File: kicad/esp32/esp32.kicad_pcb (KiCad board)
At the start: 2 copper layers, 67.5 x 101.7 mm, 42 parts, among them J101 RJ45, J102 NodeMCU, J103 Annunciator, SW201 B3F-1150, SW301 B3F-1150, SW401 B3F-1150, U101 74LS14, X101 Mouse Bites, X102 Mouse Bites, X103 Mouse Bites, X104 Mouse Bites

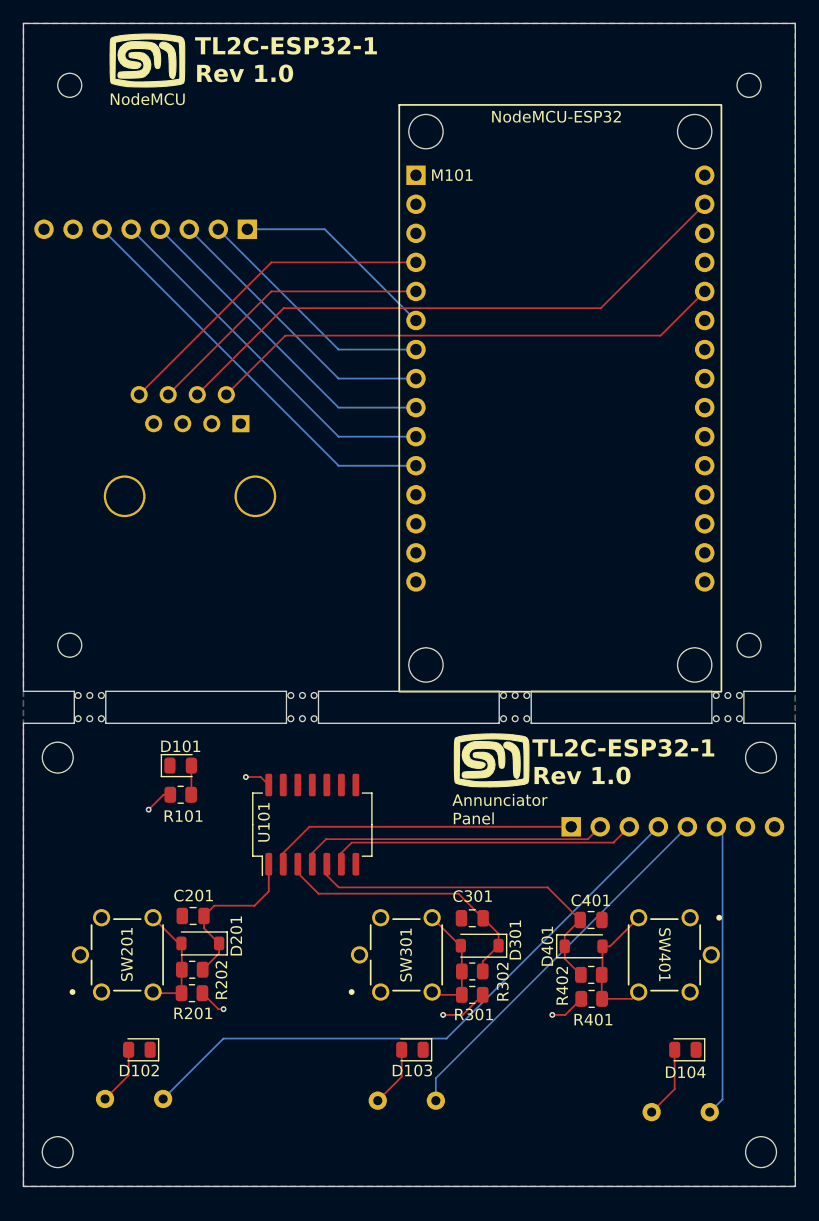
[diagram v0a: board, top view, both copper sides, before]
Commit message: Created the front panel artwork with drill marks
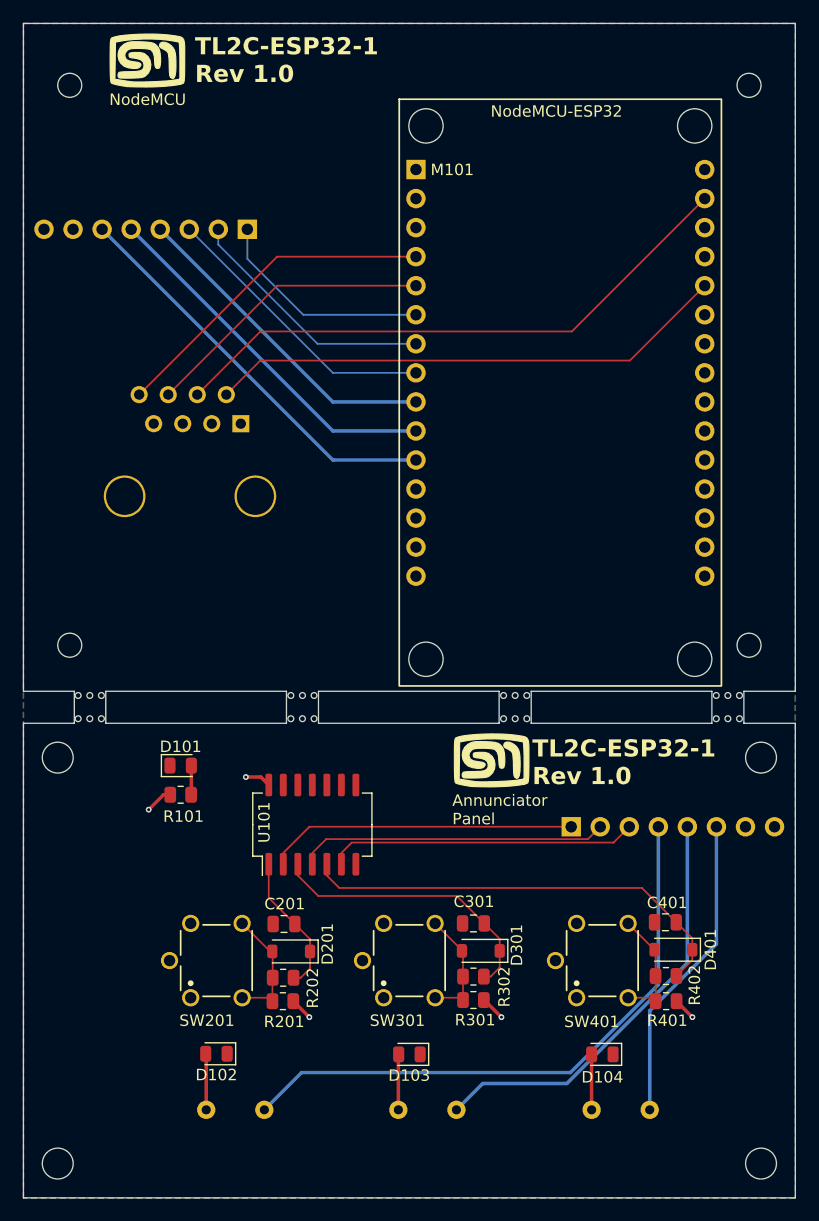
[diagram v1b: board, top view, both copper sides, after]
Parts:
- moved SW201 10.4 mm to (41.9, 107.0)
- moved R102 8.90 mm to (41.0, 120.0)
- moved SW401 8.54 mm to (75.6, 107.0), turned to 90 degrees
- moved D201 7.98 mm to (48.4, 106.2)
- moved R201 7.98 mm to (47.7, 110.5)
- moved C201 7.98 mm to (47.8, 103.8)
- moved R202 7.98 mm to (47.7, 108.5)
- moved D401 7.86 mm to (81.8, 106.0), turned to 180 degrees
- moved D104 7.27 mm to (75.6, 115.1)
- moved D102 6.75 mm to (41.9, 115.1)
- moved R402 6.53 mm to (81.2, 108.3), turned to 180 degrees
- moved R401 6.52 mm to (81.2, 110.5), turned to 180 degrees
- moved C401 6.50 mm to (81.1, 103.6), turned to 180 degrees
- moved R104 5.25 mm to (74.7, 120.0)
- moved SW301 3.72 mm to (58.8, 107.0)
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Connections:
- J101 pad 1: unconnected-(J101-Pad1) -> GND
- J101 pad 3: unconnected-(J101-Pad3) -> GND
- J101 pad 5: unconnected-(J101-Pad5) -> GND
- J101 pad 7: unconnected-(J101-Pad7) -> GND
- U101 pad 10: (no net) -> unconnected-(U101-Pad10)
- U101 pad 11: (no net) -> unconnected-(U101-Pad11)
- U101 pad 12: (no net) -> unconnected-(U101-Pad12)
- U101 pad 13: (no net) -> unconnected-(U101-Pad13)
- U101 pad 8: (no net) -> unconnected-(U101-Pad8)
- U101 pad 9: (no net) -> unconnected-(U101-Pad9)
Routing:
- net /Zone 3 Enable/ZONE_GPIO: track 30.7 -> 39.1 mm
- net /Zone2_ACTIVE: track 65.5 -> 69.6 mm
- net +3V3: track 14.4 -> 10.8 mm
- net /Zone 1 Enable/ZONE_GPIO: track 14.8 -> 12.4 mm
- net Net-(D401-A): track 12.3 -> 10.3 mm
- net Net-(D104-A): track 6.28 -> 4.85 mm
- net /Zone3_ACTIVE: track 61.6 -> 63.0 mm
- net /ZONE3_BTN: track 52.3 -> 51.1 mm
- net /Zone 2 Enable/ZONE_GPIO: track 24.4 -> 25.2 mm
- net /Zone1_ACTIVE: track 82.0 -> 81.4 mm
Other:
- board size 67.5 x 101.7 mm -> 67.5 x 102.7 mm
- board text added: "1"
- board text added: "2"
- board text added: "3"
- board text added: "TL2C ESP32 1"
- board text added: "ZONES"

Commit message: Pin reassignments after starting the firmware
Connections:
- M101 pad 10: /Zone2_ACTIVE -> unconnected-(M101-TOUCH7/ADC17/D27-Pad10)
- M101 pad 11: /Zone3_ACTIVE -> /Zone1_ACTIVE
- M101 pad 13: unconnected-(M101-SPI-MISO/TOUCH4/ADC14/D13-Pad13) -> /Zone2_ACTIVE
- M101 pad 18: unconnected-(M101-SPI-SS/TOUCH3/ADC13/D15-Pad18) -> /Zone3_ACTIVE
- M101 pad 4: /~{SLEEP} -> unconnected-(M101-ADC6/D34-Pad4)
- M101 pad 5: /STATE_INTERRUPT -> /~{SLEEP}
- M101 pad 6: /ZONE1_BTN -> /STATE_INTERRUPT
- M101 pad 7: /ZONE2_BTN -> /ZONE1_BTN
- M101 pad 8: /ZONE3_BTN -> /ZONE2_BTN
- M101 pad 9: /Zone1_ACTIVE -> /ZONE3_BTN
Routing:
- net /Zone3_ACTIVE: track 63.0 -> 91.5 mm
- net /Zone2_ACTIVE: track 69.6 -> 73.0 mm
- net /Zone1_ACTIVE: track 81.4 -> 83.5 mm
- net /~{SLEEP}: track 29.2 -> 28.2 mm
- net /ZONE3_BTN: track 51.1 -> 52.2 mm
- net /STATE_INTERRUPT: track 25.6 -> 24.6 mm

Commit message: Completed the release for OSH Park
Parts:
- moved Lg102 1.99 mm to (64.0, 90.0)
- moved H103 1.36 mm to (88.5, 78.0)
- moved H104 1.36 mm to (29.1, 78.0)
- moved H106 1.22 mm to (29.0, 124.0)
- moved H107 1.22 mm to (88.5, 124.0)
- moved H105 1.12 mm to (29.0, 89.7)
- moved H108 1.12 mm to (88.5, 89.7)
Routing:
- net /ZONE2_BTN: track 48.6 -> 52.4 mm
- net /ZONE3_BTN: track 52.2 -> 55.7 mm
- net /ZONE1_BTN: track 45.1 -> 47.3 mm
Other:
- board text added: "Test Mode"

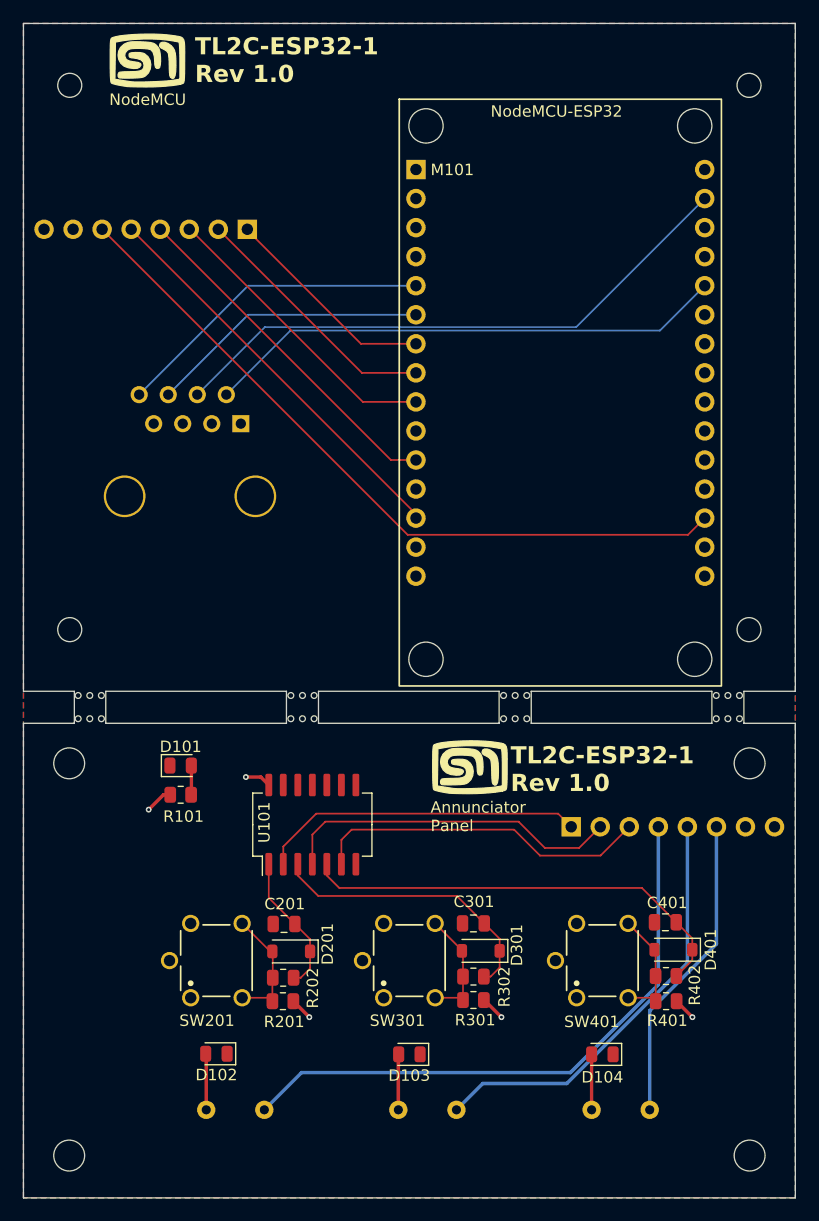
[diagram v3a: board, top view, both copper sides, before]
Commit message: Created rev 1.01 - Addes some more labels and annotations
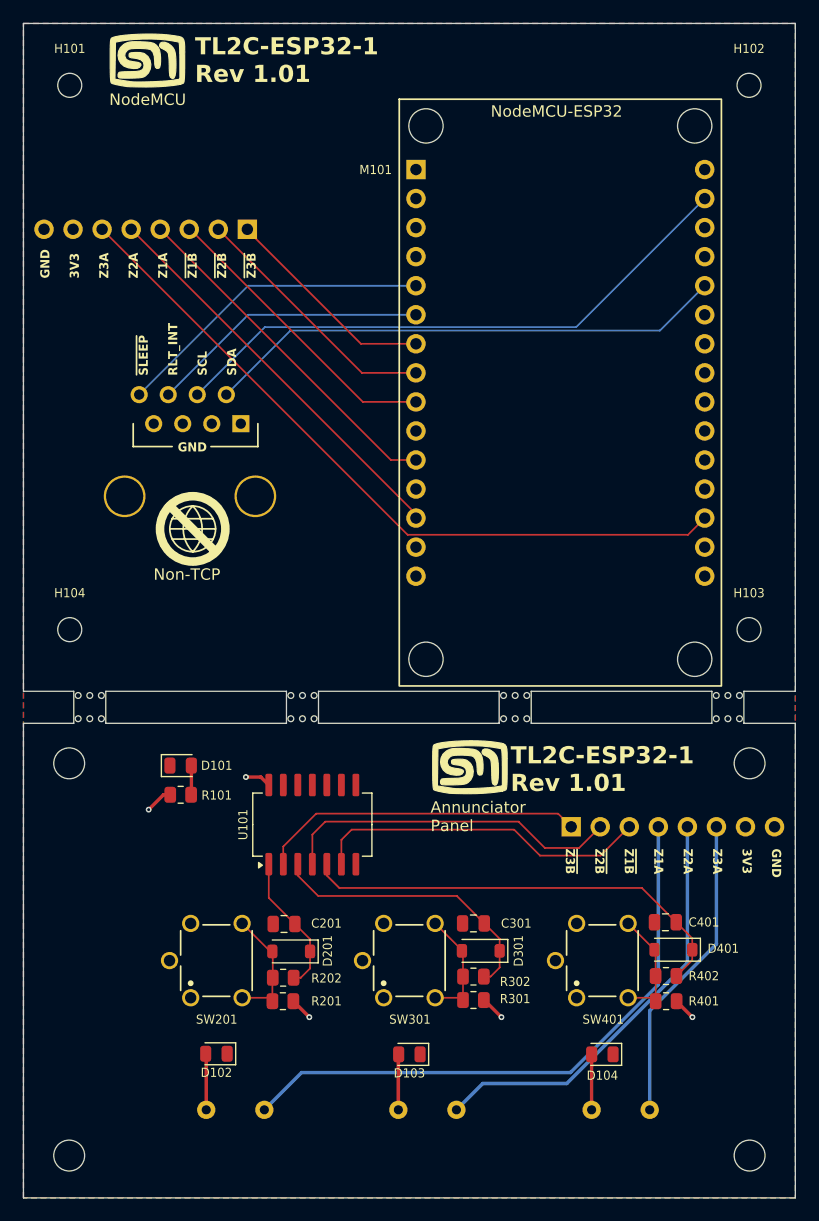
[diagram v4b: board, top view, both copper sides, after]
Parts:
- added Lg103: SM Logo, sjm-mechanical:MyBasic_rounded_50_1_USER5, F.Cu at (36.0, 90.4)
- added Lg104: Non-TCP, sjm-mechanical:Non_TCP, F.Cu at (39.8, 69.2)
- added Lg105: Non-TCP, sjm-mechanical:Non_TCP, B.Cu at (39.7, 78.1)
- added Lg106: SM Logo, sjm-mechanical:MyBasic_rounded_50_1, B.Cu at (80.0, 28.3)
- added Lg107: SM Logo, sjm-mechanical:MyBasic_rounded_50_1, B.Cu at (81.5, 90.0)
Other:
- board text added: "GND"
- board text added: "GND 3V3 Z3A Z2A Z1A ~{Z1B} ~{Z2B} ~{Z3B}"
- board text added: "TL2C ESP32-1"
- board text added: "TL2C-ESP32-1 Rev 1.01"
- board text added: "~{SLEEP} RLT_INT SCL SDA"
- board text removed: "TL2C ESP32 1"
- board text removed: "TL2C-ESP32-1 Rev 1.0"

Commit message: Reseated the RJ45
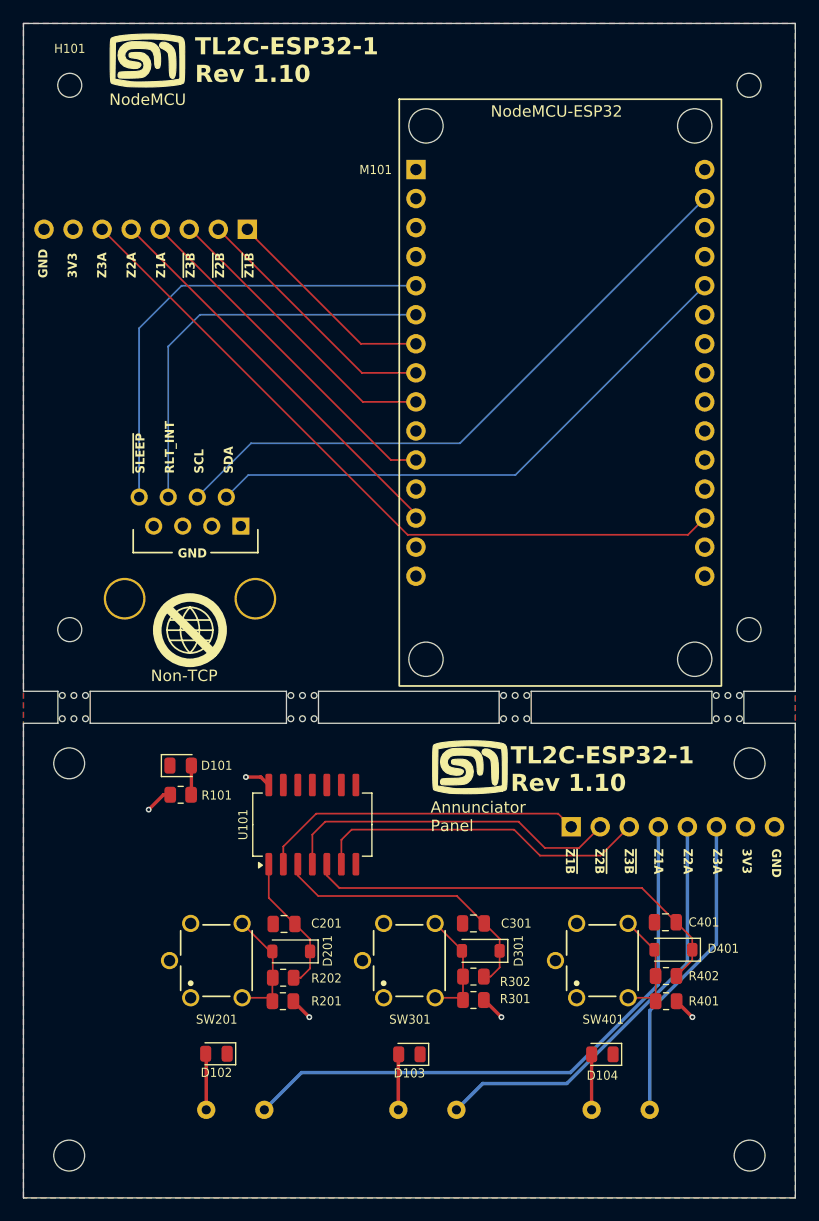
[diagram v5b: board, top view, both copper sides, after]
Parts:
- R201, R301, R401: value 51κΩ -> 47κΩ
- R202, R302, R402: value 21kΩ -> 470Ω
- moved J101 8.96 mm to (35.1, 66.4)
- moved Lg104 8.86 mm to (39.6, 78.1)
- moved X101 1.39 mm to (29.4, 84.8)
- moved Lg105 0.15 mm to (39.6, 78.1)
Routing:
- net /~{SLEEP}: track 28.2 -> 40.5 mm
- net /STATE_INTERRUPT: track 24.6 -> 36.0 mm
- net /I2C_SDA: track 45.8 -> 49.5 mm
- net /I2C_SCL: track 51.5 -> 55.2 mm
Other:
- outline, holes or cut-outs redrawn
- board text added: "GND 3V3 Z3A Z2A Z1A ~{Z3B} ~{Z2B} ~{Z1B}"
- board text added: "TL2C-ESP32-1 Rev 1.10"
- board text removed: "GND 3V3 Z3A Z2A Z1A ~{Z1B} ~{Z2B} ~{Z3B}"
- board text removed: "TL2C-ESP32-1 Rev 1.01"

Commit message: Adding some documentation
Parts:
- C201, C301, C401: value 1μF -> 0.1μF
- R201, R301, R401: value 47κΩ -> 4.7κΩ

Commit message: Updated the artwork and documentation
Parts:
- R201, R301, R401: value 4.7κΩ -> 10κΩ
- R202, R302, R402: value 470Ω -> 10κΩ
- U101: value 74LS14 -> 74HC14
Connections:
- U101 pad 6: /ZONE3_BTN -> unconnected-(U101-Pad6)
